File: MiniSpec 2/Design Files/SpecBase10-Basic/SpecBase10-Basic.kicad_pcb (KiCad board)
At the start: 2 copper layers, 65 x 95 mm, 18 parts, among them J1 M20-8770642R, J2 M20-8770642R, J3 Conn_01x04_Male

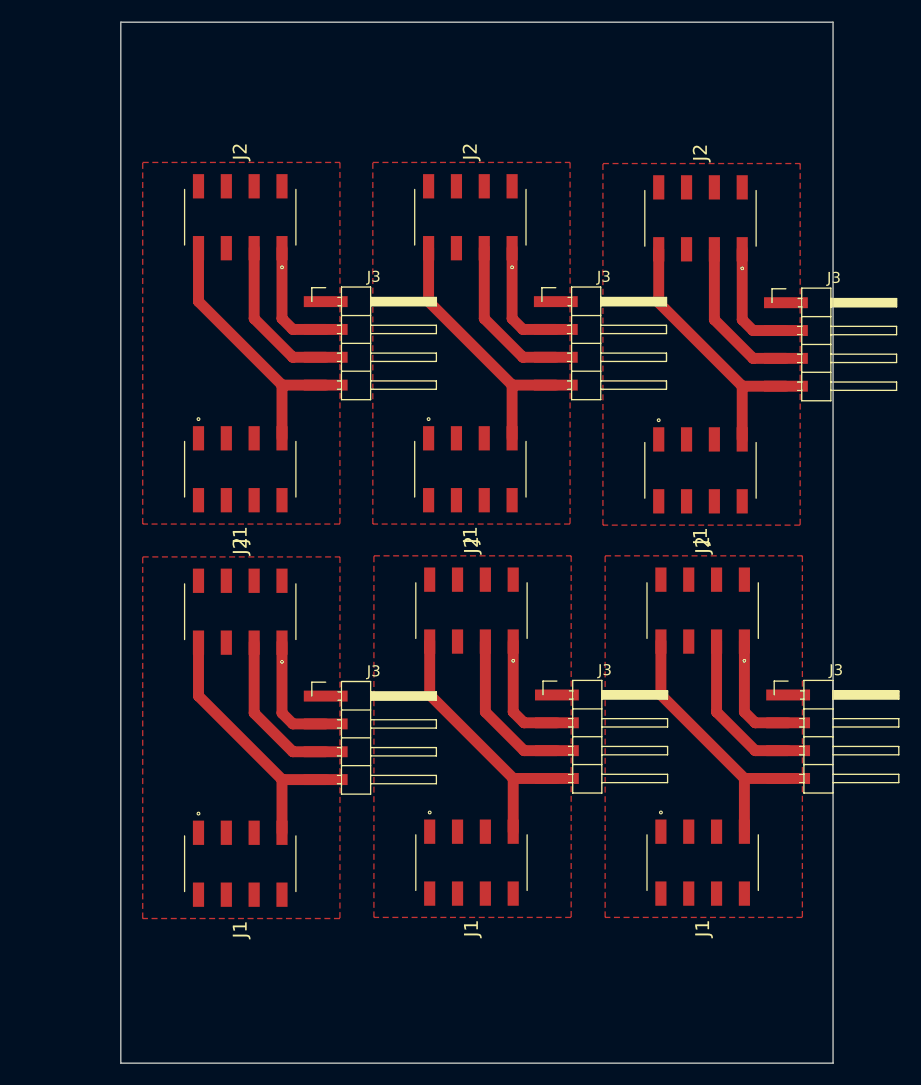
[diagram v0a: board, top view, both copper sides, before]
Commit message: Finished I2C Bus Board, added raw data of spec readings
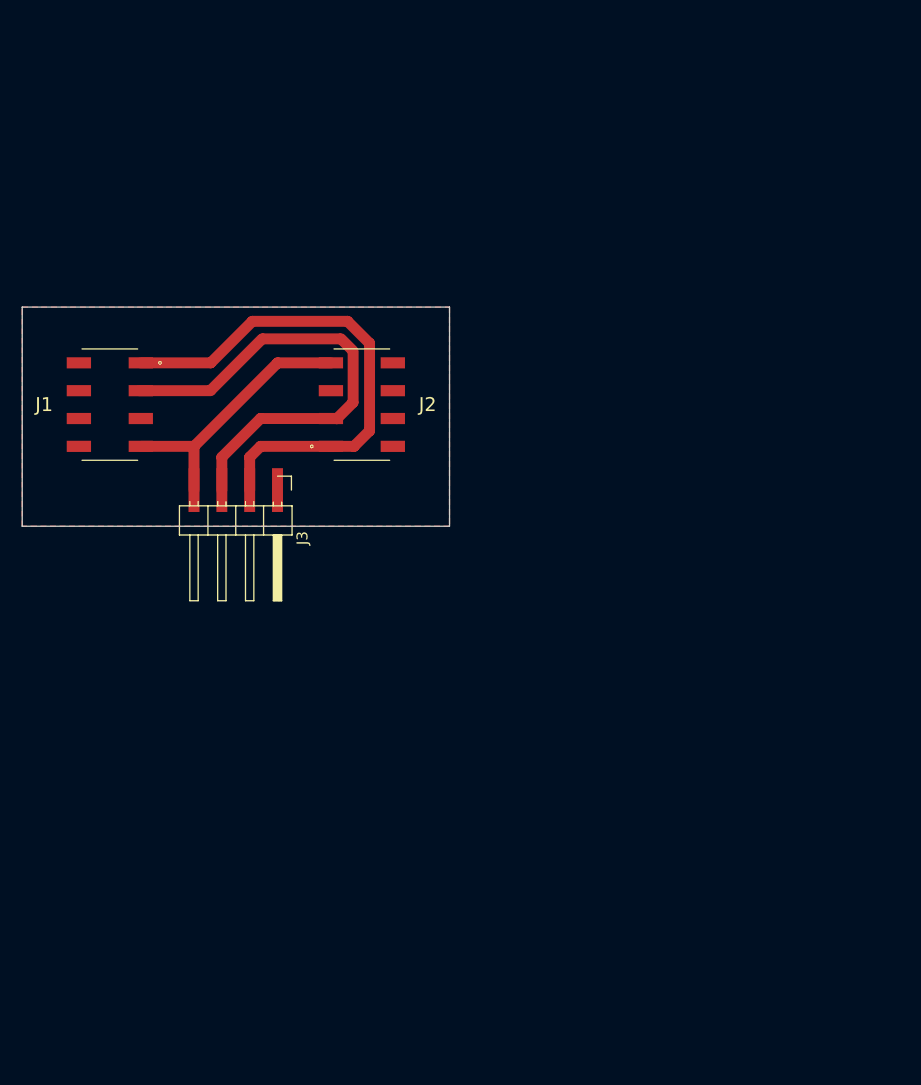
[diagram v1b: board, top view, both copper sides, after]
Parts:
- removed the J1 at (163.1, 140.7)
- removed the J1 at (142.0, 140.7)
- removed the J1 at (120.9, 140.8)
- removed the J1 at (162.9, 104.9)
- removed the J1 at (141.9, 104.8)
- removed the J2 at (163.1, 117.7)
- removed the J2 at (142.0, 117.7)
- removed the J2 at (120.9, 117.8)
- removed the J2 at (162.9, 81.9)
- removed the J2 at (141.9, 81.8)
- removed the J3 at (170.9, 125.4)
- removed the J3 at (149.8, 125.4)
- removed the J3 at (128.7, 125.5)
- removed the J3 at (170.7, 89.6)
- removed the J3 at (149.7, 89.5)
- moved J2 20.4 mm to (132.0, 98.9), turned to 270 degrees
- moved J3 17.8 mm to (124.3, 106.7), turned to 270 degrees
- moved J1 13.3 mm to (109.0, 98.9), turned to 90 degrees
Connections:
- J1 pad 1: (no net) -> SDA
- J1 pad 2: (no net) -> GND
- J1 pad 3: (no net) -> SCL
- J1 pad 4: (no net) -> GND
- J1 pad 6: (no net) -> GND
- J1 pad 8: (no net) -> GND
- J2 pad 2: (no net) -> GND
- J2 pad 4: (no net) -> GND
- J2 pad 6: (no net) -> GND
- J2 pad 8: (no net) -> GND
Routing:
- net +3V3: track 147.0 -> 24.5 mm
- net SCL: track 86.5 -> 43.0 mm
- net SDA: track 65.0 -> 46.2 mm
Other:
- board size 65 x 95 mm -> 39 x 20 mm
